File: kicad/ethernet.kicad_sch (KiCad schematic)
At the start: 6 parts, among them U8 TPD4EUSB30DQAR, U9 TPD4EUSB30DQAR

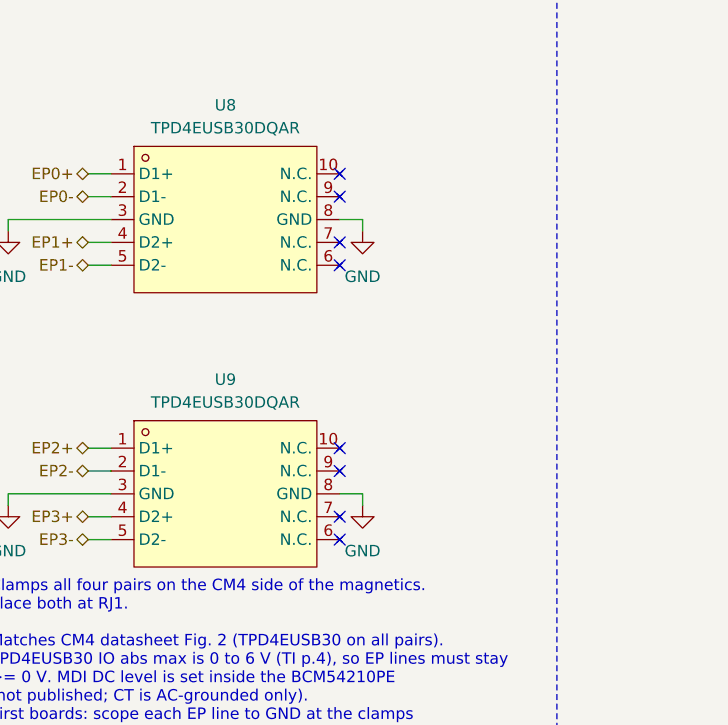
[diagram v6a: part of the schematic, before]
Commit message: PCB: route USB section and Ethernet, rework ESD flow-through wiring
USB:
- Connect C16 and nEXTRST (hub pin 26 to CM4 pin 100 under the module);
  re-route HS_IND to free pin 26; GND via for TP8.
- Restore 3D models dropped by API rotations; fix USBC1 power pads and
  peg holes and USB1 silkscreen (footprint fixes in parts).
- U5: HSD2 now flows through pins 4->7 and 5->6; pins 1, 2, 9, 10
  no-connect. U5 rotated and moved to suit.

Ethernet:
- U8/U9 N.C. pins carry the line (flow-through, like U6); their sheet
  symbol copy types those pins passive so ERC passes.
- Place U8/U9 in line with RJ1 pin gaps, C23 on the centre tap.
- Route all four pairs on ETH_100_OHM (0.11/0.13): outer-row pairs on
  F.Cu (EP2 hops under EP3), inner-row pairs via a B.Cu bundle, with the
  P/N and pair-order swaps done at the vias.
- LEDs on B.Cu to R18/R19 (positions swapped), CM4 GND pins 1/2, 7/8,
  13/14 via'd between the connector rows, RJ1 chassis pins tied.
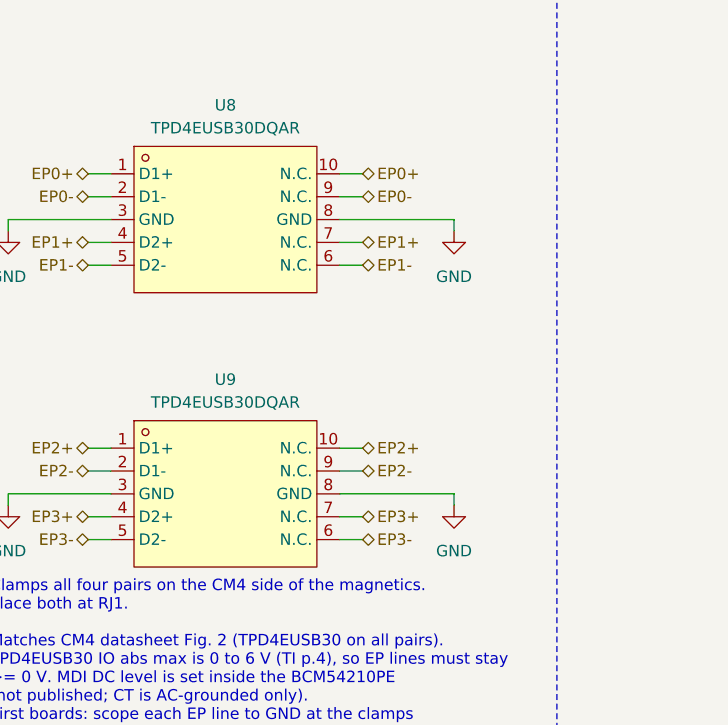
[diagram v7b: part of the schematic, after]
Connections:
- net EP0+: now also U8.10 (N.C.)
- net EP0-: now also U8.9 (N.C.)
- net EP1+: now also U8.7 (N.C.)
- net EP1-: now also U8.6 (N.C.)
- net EP2+: now also U9.10 (N.C.)
- net EP2-: now also U9.9 (N.C.)
- net EP3+: now also U9.7 (N.C.)
- net EP3-: now also U9.6 (N.C.)
- no-connect marks 8 -> 0
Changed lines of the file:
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@@
 		(color 0 0 0 0)
 	)
-	(no_connect
-		(at 215.9 71.12)
-	)
-	(no_connect
-		(at 215.9 60.96)
-	)
-	(no_connect
-		(at 215.9 93.98)
-	)
-	(no_connect
-		(at 215.9 63.5)
-	)
-	(no_connect
-		(at 215.9 68.58)
-	)
-	(no_connect
-		(at 215.9 91.44)
-	)
-	(no_connect
-		(at 215.9 99.06)
-	)
-	(no_connect
-		(at 215.9 101.6)
-	)
 	(wire
 		(pts
@@
 	(wire
 		(pts
-			(xy 215.9 66.04) (xy 218.44 66.04)
+			(xy 215.9 66.04) (xy 228.6 66.04)
 		)
 		(stroke
@@
 	(wire
 		(pts
-			(xy 215.9 96.52) (xy 218.44 96.52)
+			(xy 215.9 96.52) (xy 228.6 96.52)
 		)
 		(stroke
@@
 	(wire
 		(pts
-			(xy 218.44 66.04) (xy 218.44 67.31)
+			(xy 228.6 66.04) (xy 228.6 67.31)
 		)
 		(stroke
@@
 	(wire
 		(pts
-			(xy 218.44 96.52) (xy 218.44 97.79)
+			(xy 228.6 96.52) (xy 228.6 97.79)
 		)
 		(stroke
@@
 	(symbol
 		(lib_id "power:GND")
-		(at 218.44 67.31 0)
+		(at 228.6 67.31 0)
 		(unit 1)
 		(body_style 1)
@@
 		(fields_autoplaced yes)
 		(property "Reference" "#PWR078"
-			(at 218.44 73.66 0)
+			(at 228.6 73.66 0)
 			(hide yes)
 			(show_name no)
@@
 		)
 		(property "Value" "GND"
-			(at 218.44 72.39 0)
+			(at 228.6 72.39 0)
 			(show_name no)
 			(do_not_autoplace no)
@@
 		)
 		(property "Footprint" ""
-			(at 218.44 67.31 0)
+			(at 228.6 67.31 0)
 			(hide yes)
 			(show_name no)
@@
 		)
 		(property "Datasheet" ""
-			(at 218.44 67.31 0)
+			(at 228.6 67.31 0)
 			(hide yes)
 			(show_name no)
@@
 		)
 		(property "Description" "Power symbol creates a global label with name \"GND\" , ground"
-			(at 218.44 67.31 0)
+			(at 228.6 67.31 0)
 			(hide yes)
 			(show_name no)
@@
 	(symbol
 		(lib_id "power:GND")
-		(at 218.44 97.79 0)
+		(at 228.6 97.79 0)
 		(unit 1)
 		(body_style 1)
@@
 		(fields_autoplaced yes)
 		(property "Reference" "#PWR081"
-			(at 218.44 104.14 0)
+			(at 228.6 104.14 0)
 			(hide yes)
 			(show_name no)
@@
 		)
 		(property "Value" "GND"
-			(at 218.44 102.87 0)
+			(at 228.6 102.87 0)
 			(show_name no)
 			(do_not_autoplace no)
@@
 		)
 		(property "Footprint" ""
-			(at 218.44 97.79 0)
+			(at 228.6 97.79 0)
 			(hide yes)
 			(show_name no)
@@
 		)
 		(property "Datasheet" ""
-			(at 218.44 97.79 0)
+			(at 228.6 97.79 0)
 			(hide yes)
 			(show_name no)
@@
 		)
 		(property "Description" "Power symbol creates a global label with name \"GND\" , ground"
-			(at 218.44 97.79 0)
+			(at 228.6 97.79 0)
 			(hide yes)
 			(show_name no)
@@
 		)
 	)
+	(wire
+		(pts
+			(xy 215.9 60.96) (xy 218.44 60.96)
+		)
+		(stroke
+			(width 0)
+			(type default)
+		)
+	)
+	(hierarchical_label "EP0+"
+		(shape bidirectional)
+		(at 218.44 60.96 0)
+		(effects
+			(font
+				(size 1.27 1.27)
+			)
+			(justify left)
+		)
+	)
+	(wire
+		(pts
+			(xy 215.9 63.5) (xy 218.44 63.5)
+		)
+		(stroke
+			(width 0)
+			(type default)
+		)
+	)
+	(hierarchical_label "EP0-"
+		(shape bidirectional)
+		(at 218.44 63.5 0)
+		(effects
+			(font
+				(size 1.27 1.27)
+			)
+			(justify left)
+		)
+	)
+	(wire
+		(pts
+			(xy 215.9 68.58) (xy 218.44 68.58)
+		)
+		(stroke
+			(width 0)
+			(type default)
+		)
+	)
+	(hierarchical_label "EP1+"
+		(shape bidirectional)
+		(at 218.44 68.58 0)
+		(effects
+			(font
+				(size 1.27 1.27)
+			)
+			(justify left)
+		)
+	)
+	(wire
+		(pts
+			(xy 215.9 71.12) (xy 218.44 71.12)
+		)
+		(stroke
+			(width 0)
+			(type default)
+		)
+	)
+	(hierarchical_label "EP1-"
+		(shape bidirectional)
+		(at 218.44 71.12 0)
+		(effects
+			(font
+				(size 1.27 1.27)
+			)
+			(justify left)
+		)
+	)
+	(wire
+		(pts
+			(xy 215.9 91.44) (xy 218.44 91.44)
+		)
+		(stroke
+			(width 0)
+			(type default)
+		)
+	)
+	(hierarchical_label "EP2+"
+		(shape bidirectional)
+		(at 218.44 91.44 0)
+		(effects
+			(font
+				(size 1.27 1.27)
+			)
+			(justify left)
+		)
+	)
+	(wire
+		(pts
+			(xy 215.9 93.98) (xy 218.44 93.98)
+		)
+		(stroke
+			(width 0)
+			(type default)
+		)
+	)
+	(hierarchical_label "EP2-"
+		(shape bidirectional)
+		(at 218.44 93.98 0)
+		(effects
+			(font
+				(size 1.27 1.27)
+			)
+			(justify left)
+		)
+	)
+	(wire
+		(pts
+			(xy 215.9 99.06) (xy 218.44 99.06)
+		)
+		(stroke
+			(width 0)
+			(type default)
+		)
+	)
+	(hierarchical_label "EP3+"
+		(shape bidirectional)
+		(at 218.44 99.06 0)
+		(effects
+			(font
+				(size 1.27 1.27)
+			)
+			(justify left)
+		)
+	)
+	(wire
+		(pts
+			(xy 215.9 101.6) (xy 218.44 101.6)
+		)
+		(stroke
+			(width 0)
+			(type default)
+		)
+	)
+	(hierarchical_label "EP3-"
+		(shape bidirectional)
+		(at 218.44 101.6 0)
+		(effects
+			(font
+				(size 1.27 1.27)
+			)
+			(justify left)
+		)
+	)
